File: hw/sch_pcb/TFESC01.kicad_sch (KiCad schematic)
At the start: 151 parts, among them P1 CONN_1, P10 Conn_01x06, P11 Conn_01x06, P2 CONN_1, P3 CONN_1, P4 CONN_1, P5 CONN_1, P6 CONN_1, P9 Conn_01x06, Q1 NTMFS5C604NLT1G, Q2 NTMFS5C604NLT1G, Q3 NTMFS5C604NLT1G, Q4 NTMFS5C604NLT1G, Q5 NTMFS5C604NLT1G, Q6 NTMFS5C604NLT1G, U1 LM5113SDE, U10 MCP1700, U2 LM5113SDE, U3 LM5113SDE, U4 AD8417, U5 AD8417, U6 AD8417, U7 STM32F405RGT6, U8 LMR16006YDDCT, U9 MCP1700, X1 ABM3B-8.000MHZ

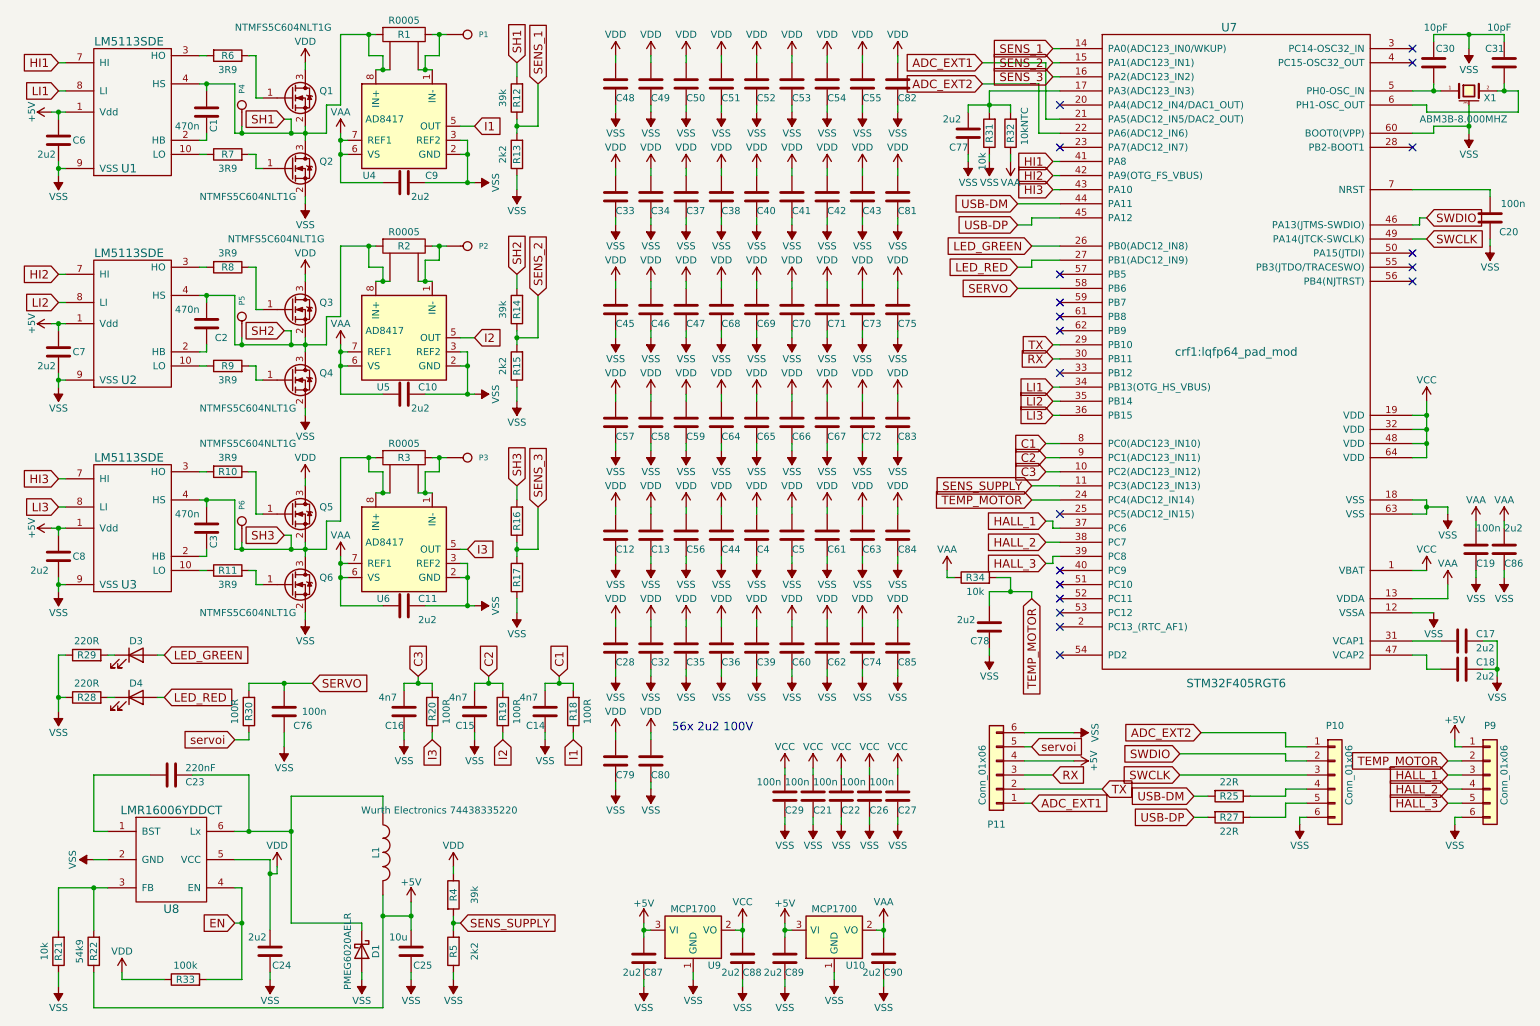
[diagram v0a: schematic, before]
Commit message: Split schematics to multiple pages.
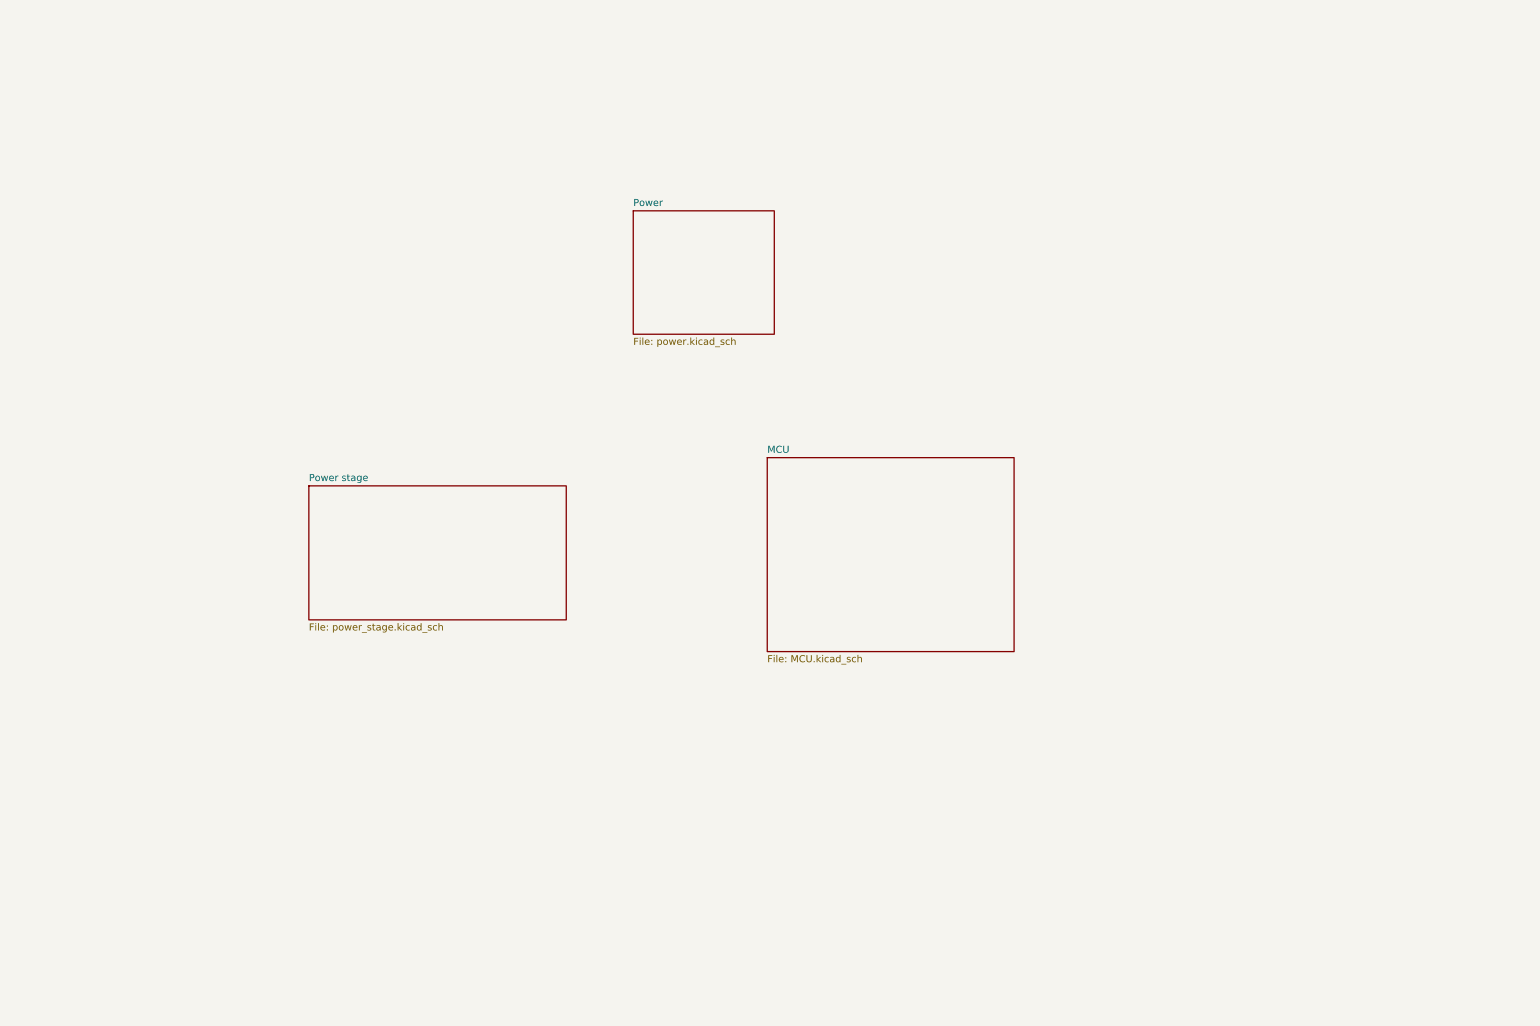
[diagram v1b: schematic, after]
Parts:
- removed C1, C2, C3: 470n, Capacitors_SMD:C_0603, symbol Device:C
- removed C10, C11, C17, C18, C6, C7, C77, C78, C8, C86, C87, C88, C89, C9, C90: 2u2, Capacitors_SMD:C_0603, symbol Device:C
- removed C12, C13, C25, C28, C32, C39, C4, C48, C5, C60, C61, C62, C63, C74, C75, C79, C80, C82, C84, C85: 10u, Resistors_SMD:R_1206, symbol Device:C
- removed C14, C15, C16: 4n7, Capacitors_SMD:C_0603, symbol Device:C
- removed C19, C20, C21, C22, C26, C27, C29: 100n, Capacitors_SMD:C_0603, symbol Device:C
- removed C23: 220nF, Resistors_SMD:R_0603, symbol Device:C
- removed C24: 2u2, Resistors_SMD:R_1206, symbol Device:C
- removed C30, C31: 10pF, Capacitors_SMD:C_0603, symbol Device:C
- removed C33, C34, C35, C36, C37, C38, C40, C41, C42, C43, C44, C45, C46, C47, C49, C50, C51, C52, C53, C54, C55, C56, C57, C58, C59, C64, C65, C66, C67, C68, C69, C70, C71, C72, C73, C81, C83: C, Resistors_SMD:R_1206, symbol Device:C
- removed C76: 100n, Resistors_SMD:R_0603, symbol Device:C
- removed D1: PMEG6020AELR, Diodes_SMD:D_SOD-123, symbol Device:D_Schottky
- removed D3, D4: LED, Resistors_SMD:R_0603, symbol Device:LED
- removed L1: Wurth Electronics 74438335220, mojaKniznica:WE-MAPI, symbol MINI VESC-rescue:INDUCTOR-RESCUE-MINI_VESC
- removed P1, P2, P3, P4, P5, P6: CONN_1, kicad_subory:prekov, symbol MINI VESC-rescue:CONN_1-RESCUE-MINI_VESC
- removed P10, P11, P9: Conn_01x06, kicad_subory:JST_ZH_1.5_6-Pin, symbol Connector_Generic:Conn_01x06
- removed Q1, Q2, Q3, Q4, Q5, Q6: NTMFS5C604NLT1G, kicad_subory:DFN5, symbol Device:Q_NMOS_GSD
- removed R1, R2, R3: R0005, mojaKniznica:2512Rv2, symbol MINI VESC-rescue:RSENS-RESCUE-MINI_VESC
- removed R10, R11, R6, R7, R8, R9: 3R9, Resistors_SMD:R_0603, symbol Device:R
- removed R12, R14, R4: 39k, Resistors_SMD:R_0603, symbol Device:R
- removed R13, R15, R17, R5: 2k2, Resistors_SMD:R_0603, symbol Device:R
- removed R16: 25k5, Resistors_SMD:R_0603, symbol Device:R
- removed R18, R19, R20, R30: 100R, Resistors_SMD:R_0603, symbol Device:R
- removed R21, R31, R34: 10k, Resistors_SMD:R_0603, symbol Device:R
- removed R22: 54k9, Resistors_SMD:R_0603, symbol Device:R
- removed R25, R27: 22R, Resistors_SMD:R_0603, symbol Device:R
- removed R28, R29: 220R, Resistors_SMD:R_0603, symbol Device:R
- removed R32: 10kNTC, Resistors_SMD:R_0603, symbol Device:R
- removed R33: 100k, Resistors_SMD:R_0603, symbol Device:R
- removed U1, U2, U3: LM5113SDE, kicad_subory:WSON10__, symbol MINI VESC-rescue:LM5001-RESCUE-MINI_VESC
- removed U10, U9: MCP1700, TO_SOT_Packages_SMD:SOT-23, symbol MINI VESC-rescue:MCP1700-RESCUE-MINI_VESC
- removed U4, U5, U6: AD8417, kicad_subory:MSOP, symbol MINI VESC-rescue:AD8418-RESCUE-MINI_VESC
- removed U7: STM32F405RGT6, crf1:lqfp64_pad_mod, symbol MINI VESC-rescue:STM32F40X_LQFP64-RESCUE-MINI_VESC
- removed U8: LMR16006YDDCT, TO_SOT_Packages_SMD:SOT-23-6, symbol MINI VESC-rescue:BD9G101G-RESCUE-MINI_VESC
- removed X1: ABM3B-8.000MHZ, mojaKniznica:5x3.2KRISTALL, symbol MINI VESC-rescue:CRYSTAL_SMD-RESCUE-MINI_VESC
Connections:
- no-connect marks 20 -> 0
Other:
- added sheet MCU (MCU.kicad_sch)
- added sheet Power (power.kicad_sch)
- added sheet Power stage (power_stage.kicad_sch)
- note removed: "56x 2u2 100V"
- company: (none) -> ThunderFly s.r.o.
- title: (none) -> TFESC01A 

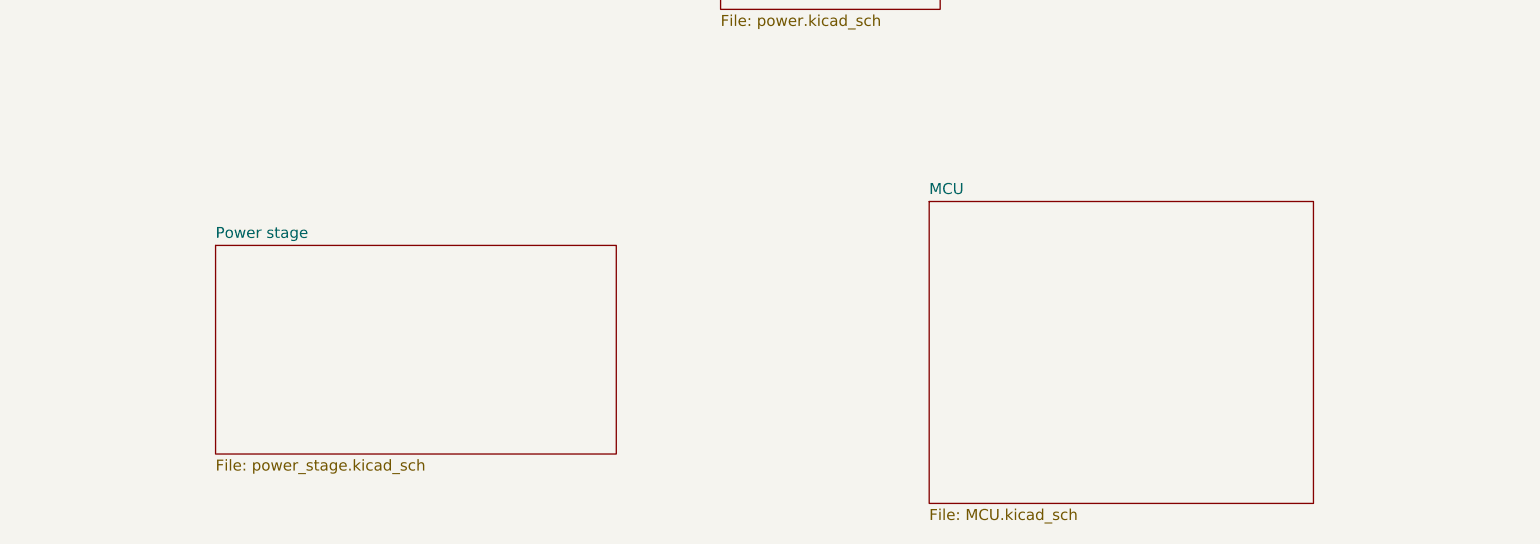
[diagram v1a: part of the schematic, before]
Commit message: CAN interface connector added #3
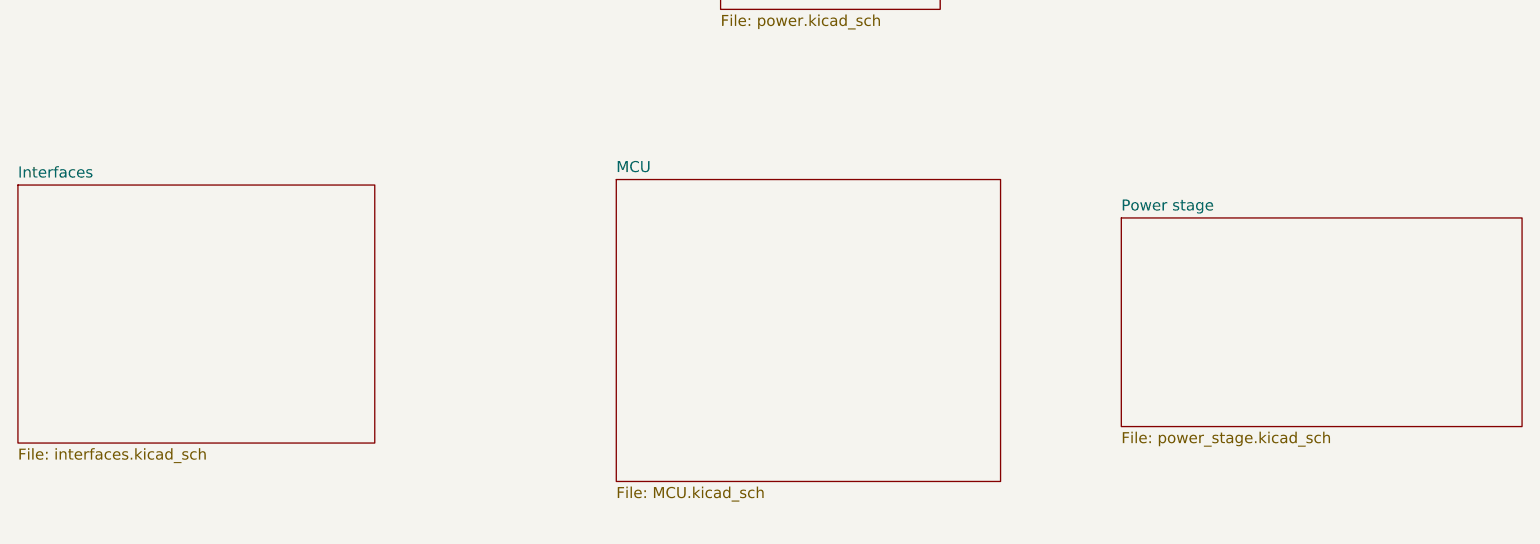
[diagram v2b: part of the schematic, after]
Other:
- added sheet Interfaces (interfaces.kicad_sch)
